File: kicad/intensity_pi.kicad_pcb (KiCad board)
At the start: 4 copper layers, 62.8 x 172 mm, 126 parts, among them J1 Input A, J2 Input B / Setpoint, J3 Monitor, J4 Output, J7 select 1, J8 Screw_Terminal_01x03, Q1 2N7002E, Q2 2N7002E, SW1 SW_SPDT, SW2 SW_SPDT, SW3 SW_SPDT, SW5 EG6100-ND, U1 LM4040DBZ-5, U10 OPA189, U11 PC817, U12 OPA189, U13 BUF634A, U14 TMUX6123, U17 TMUX6123, U18 OPA189, U19 L7815, U2 LM4040DBZ-5, U20 OPA189, U21 OPA189, U22 4x Comparator, U23 L7915, U3 INA849, U4 INA849, U5 OPA189, U7 OPA189, U8 BUF634A, U9 LM317_TO-252

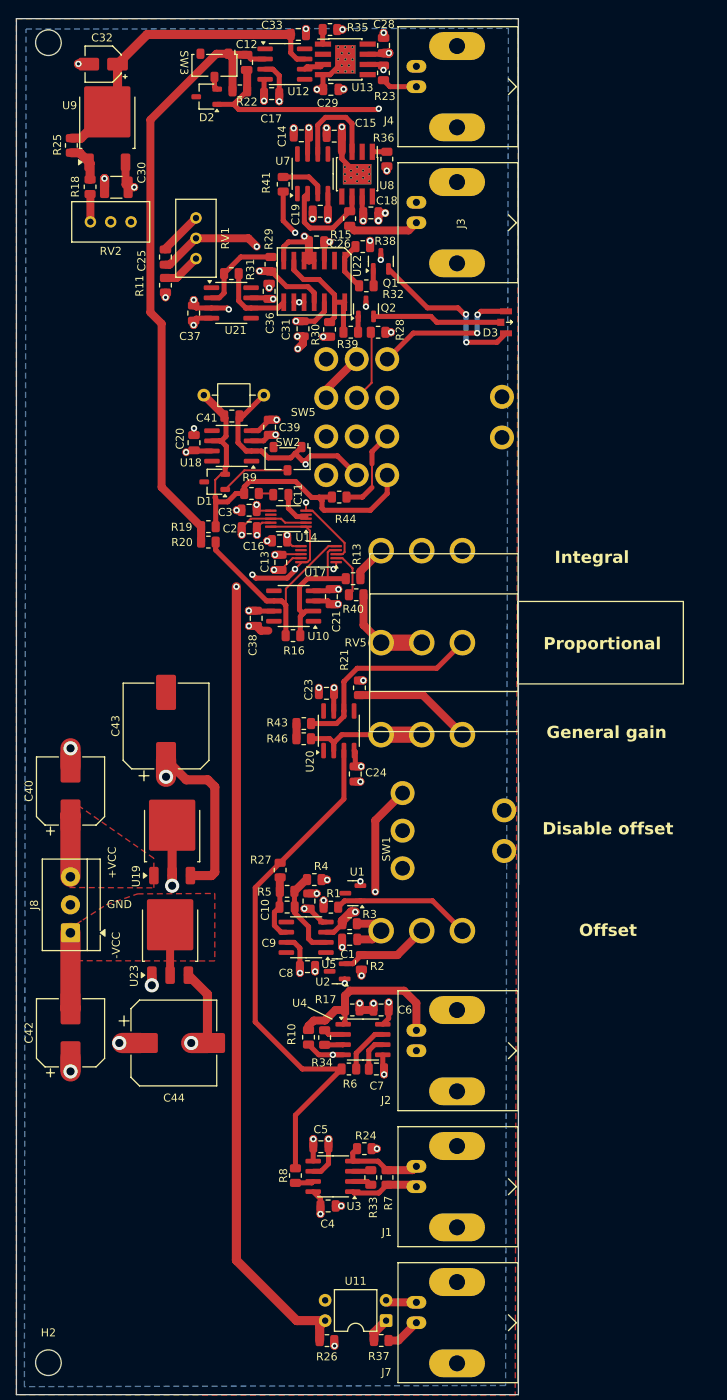
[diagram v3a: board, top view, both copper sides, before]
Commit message: Removal of antennas and other changes
The following edits has been made:
1) Simplification of certain critical traces
2) Removal of all antennas. Antennas are large traces connected to high
   impedance nodes. I'm quite strict about what high impedance means.
   Anything larger than a few Ohm can be considered high impedance.
3) Added labels most silkscreen labels where outside the physical board
   area
4) Added a thermal area to force

TO DO:
1) Add explanation near to all switches and trimpots
2) Check DRC
3) Add some GND vias
4) Check very carefully gerbers to see if any obvious manifacturing
   issue emerges
5) Send gerbers to fabrication.
6) Consider OPA209 or OPA140 for some of the opamps in the board.
One of the design choices of this board is that some opamps don't have
resistors for input current compensation. This is related to the choice
of the OPA189 for all board opamps (OPA189 has pA input current). It
turns out that for precision opamps manufacturers are starting to
discourage the use of resistors. Look at this [note](https://www.analog.com/en/resources/analog-dialogue/studentzone/studentzone-june-2017.html)
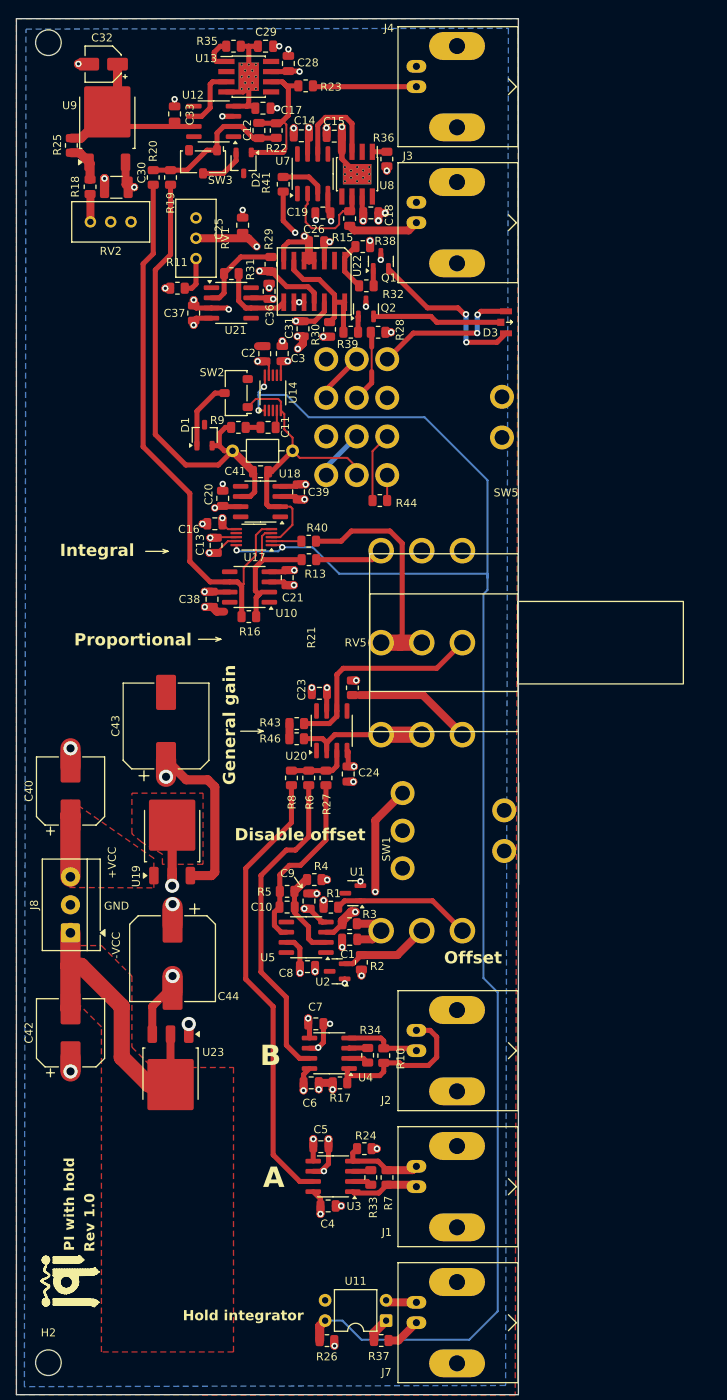
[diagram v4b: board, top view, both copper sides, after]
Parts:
- added REF**: , Custom_Footprints:JQI_LOGO_POSITIVE-SILKSCREEN, F.Cu at (-40.0, 68.3)
- moved R8 49.7 mm to (-15.6, 1.91)
- moved R20 46.1 mm to (-32.9, -73.2), turned to 90 degrees
- moved R19 43.9 mm to (-30.7, -73.2), turned to 90 degrees
- moved R6 36.7 mm to (-13.5, 1.91), turned to 90 degrees
- moved C2 21.9 mm to (-19.0, -51.1), turned to 90 degrees
- moved C3 20.0 mm to (-16.8, -51.1), turned to -90 degrees
- moved C33 18.4 mm to (-30.2, -81.1), turned to 90 degrees
- moved U23 17.5 mm to (-30.7, 39.0), turned to -90 degrees
- moved U14 15.8 mm to (-17.9, -46.2), turned to 90 degrees
- moved R27 12.9 mm to (-11.3, 1.91)
- moved C6 12.6 mm to (-13.2, 40.0), turned to 0 degrees
- moved U13 12.3 mm to (-21.0, -85.7)
- moved R35 12.2 mm to (-22.9, -89.6)
- moved SW3 12.1 mm to (-26.7, -75.1)
- moved C28 12.1 mm to (-16.0, -87.4)
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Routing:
- net Net-(U14C-SEL1): track 127.0 -> 206.1 mm
- net Net-(SW3-A): track 78.3 -> 19.5 mm
- net Net-(U20-+): track 66.5 -> 7.85 mm
- net Input_A: track 2.29 -> 56.4 mm
- net Net-(R16-Pad2): track 26.9 -> 71.0 mm
- net Input_B: track 6.26 -> 40.5 mm
- net Net-(D1-A): track 50.2 -> 83.3 mm
- net -V_DC_unregulated: track 15.8 -> 38.1 mm
- net Net-(R40-Pad1): track 12.0 -> 29.5 mm
- net Vlim+: track 38.1 -> 22.1 mm
- net GND: track 99.3 -> 84.0 mm, vias 46 -> 50
- net Internal_setpoint: track 8.10 -> 22.8 mm
- net Net-(D2-K): track 33.0 -> 20.1 mm, vias 2 -> 0
- net Net-(J4-In): track 4.45 -> 13.0 mm
- net Error_signal: track 97.1 -> 104.1 mm
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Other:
- board text added: "A"
- board text added: "B"
- board text added: "Hold integrator"
- board text added: "PI with hold"
- board text added: "Rev 1.0"

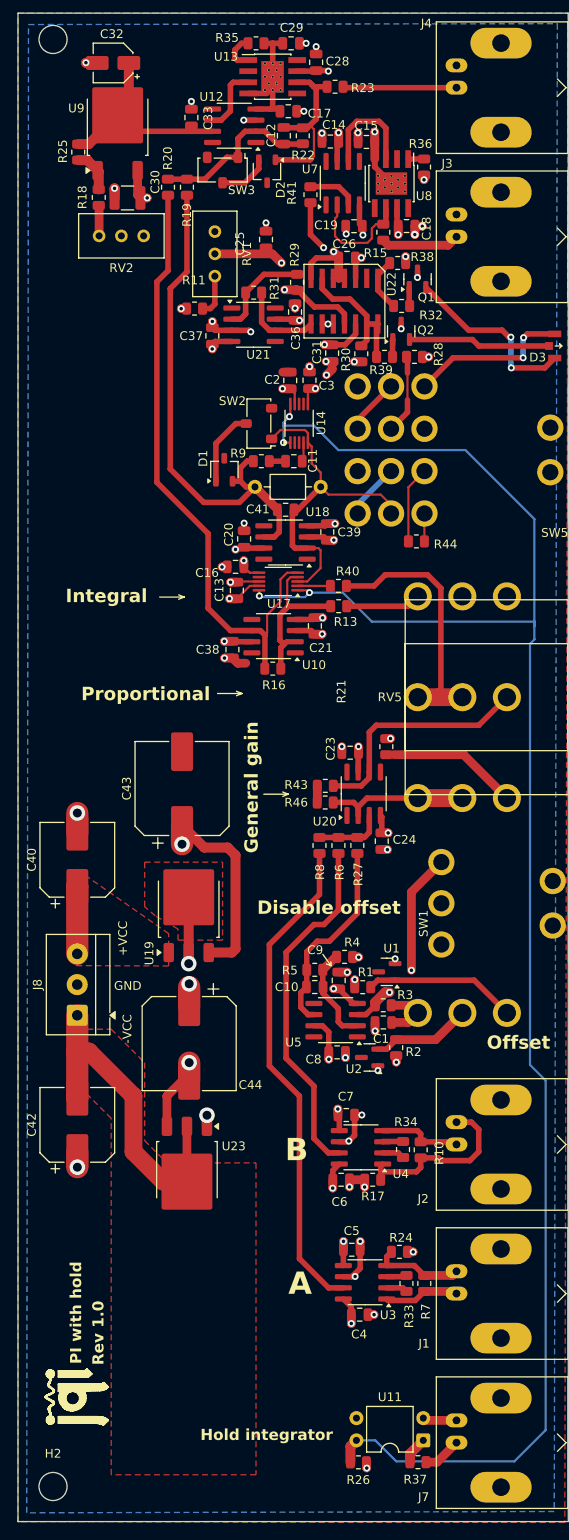
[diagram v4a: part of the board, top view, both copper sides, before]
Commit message: fixing missing traces and adding additional vias
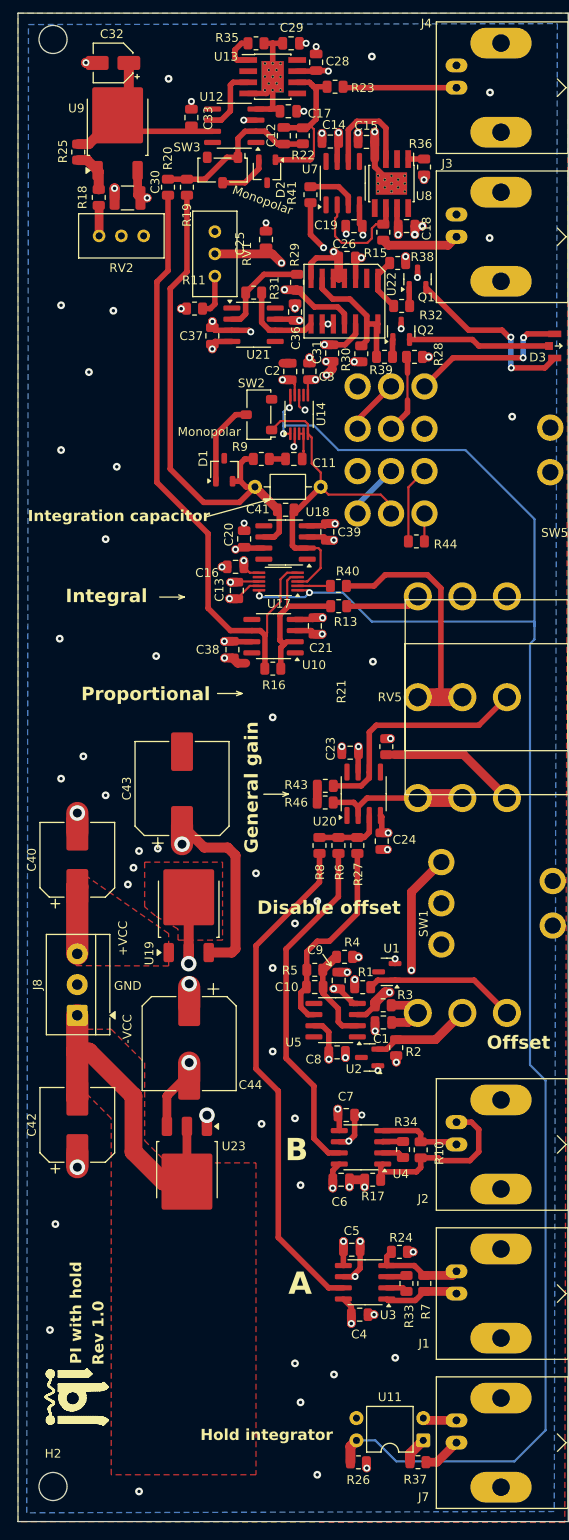
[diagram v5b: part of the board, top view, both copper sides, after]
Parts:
- moved C2 1.02 mm to (-19.0, -52.1)
- moved C3 1.02 mm to (-16.8, -52.2)
- moved SW2 1.02 mm to (-22.5, -47.2)
- moved U14 1.02 mm to (-17.9, -47.2)
- moved C11 0.25 mm to (-18.5, -42.2)
- moved R9 0.25 mm to (-22.2, -42.2)
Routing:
- net GND: track 84.0 -> 87.0 mm, vias 50 -> 90
- net Net-(C11-Pad1): track 2.18 -> 3.44 mm
- net Input_A: track 56.4 -> 57.6 mm
- net Net-(SW2-A): track 38.1 -> 39.1 mm
- net Net-(D1-K): track 8.70 -> 9.72 mm
- net Input_B: track 40.5 -> 39.9 mm
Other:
- board text added: "Integration capacitor"
- board text added: "Monopolar"

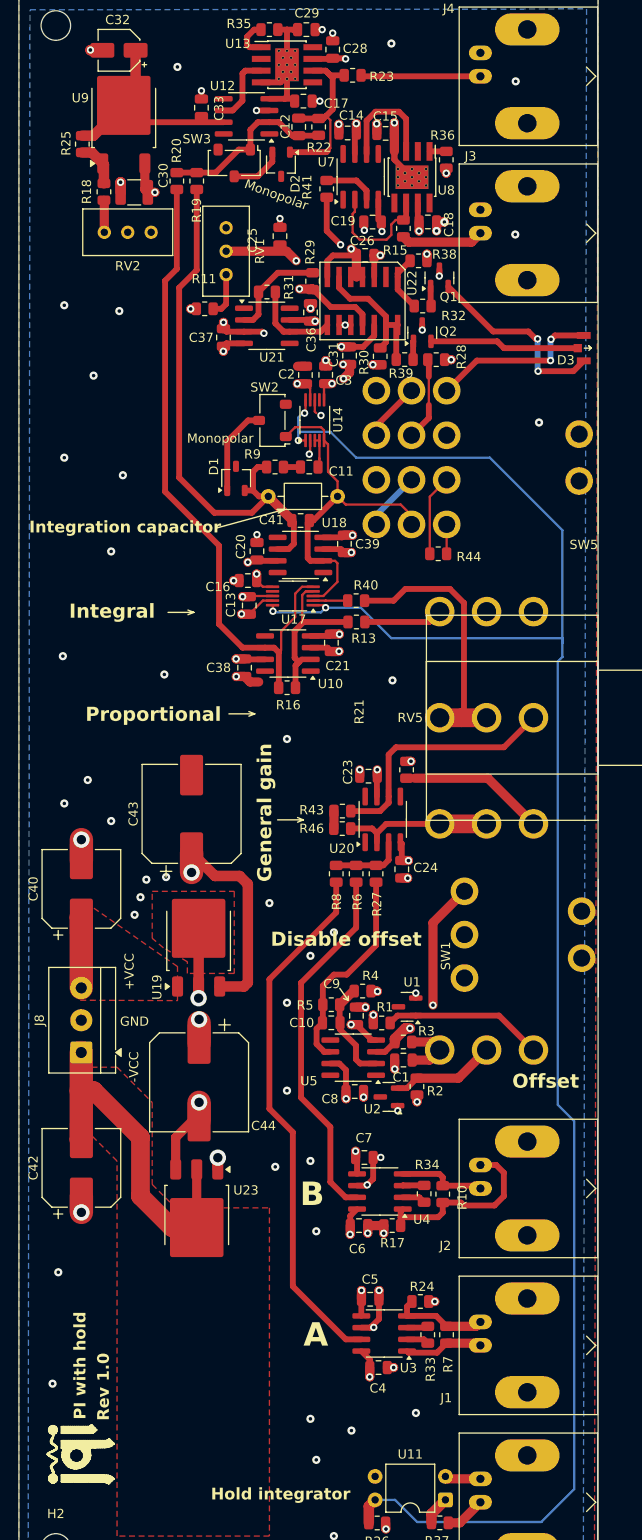
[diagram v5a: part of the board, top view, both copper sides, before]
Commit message: V1.1, Fixedincorrect footprints for Green/Red LED, Diodes, Mosfets, Flipped Input A/B Polarity, Potentiometer labels, Incorrect part nos for V regulators. No functionality changes
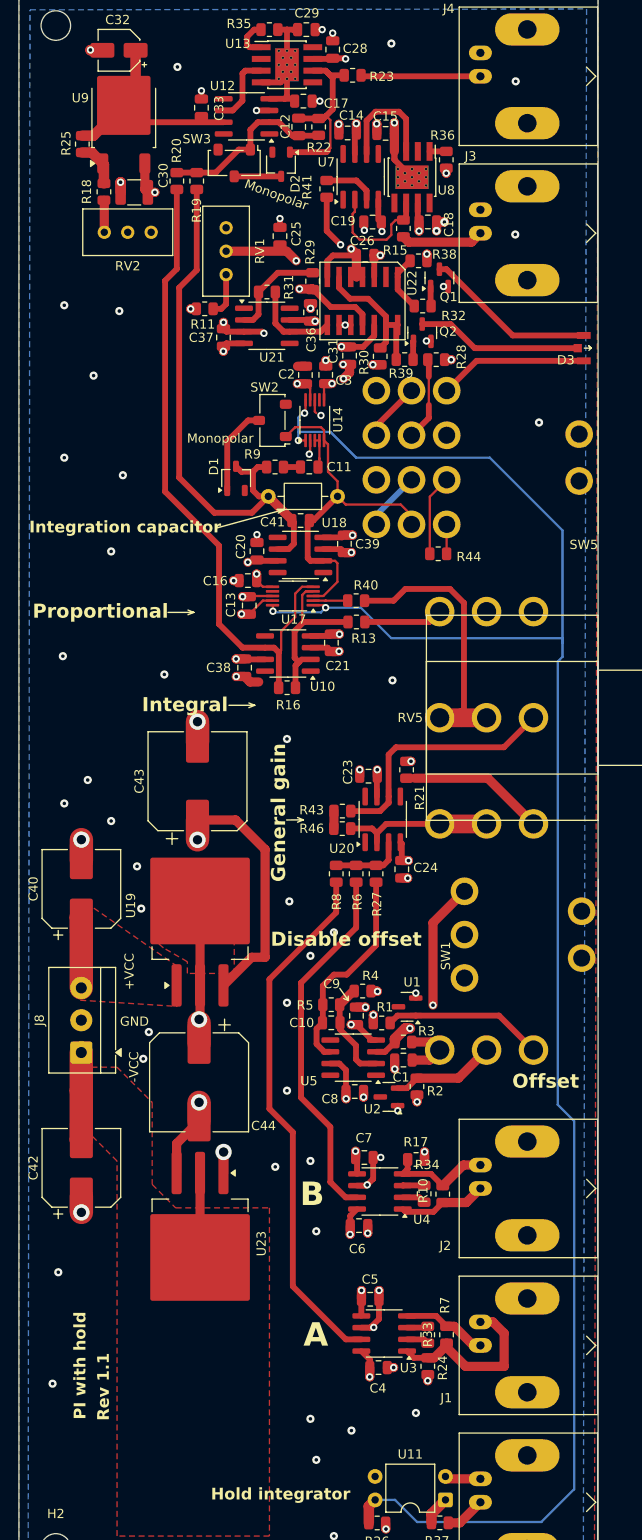
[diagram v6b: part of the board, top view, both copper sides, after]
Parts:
- removed REF**: , Custom_Footprints:JQI_LOGO_POSITIVE-SILKSCREEN
- SW5: value EG6100-ND -> SW_DP3T
- U19, U23: footprint Package_TO_SOT_SMD:TO-252-3_TabPin2 -> Package_TO_SOT_SMD:TO-263-3_TabPin2
- moved R17 7.62 mm to (-6.97, 32.9), turned to 180 degrees
- moved R24 7.06 mm to (-5.70, 55.3), turned to 90 degrees
- moved C43 3.60 mm to (-30.6, -8.12)
- moved U23 3.02 mm to (-30.4, 42.0)
- moved U19 2.73 mm to (-30.4, 6.35)
- turned R10 to -90 degrees
- turned R7 to 90 degrees
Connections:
- D1 pad 2: Net-(D1-A) -> (no net)
- D1 pad 3: (no net) -> Net-(D1-A)
- D2 pad 2: Net-(D2-A) -> (no net)
- D2 pad 3: (no net) -> Net-(D2-A)
- Q1 pad 2: Net-(D3-K1) -> GND
- Q1 pad 3: GND -> Net-(D3-K1)
- Q2 pad 2: Net-(D3-K2) -> GND
- Q2 pad 3: GND -> Net-(D3-K2)
- U3 pad 1: Net-(J1-In) -> Net-(J1-Ext)
- U3 pad 4: Net-(J1-Ext) -> Net-(J1-In)
- U4 pad 1: Net-(J2-Ext) -> Net-(J2-In)
- U4 pad 4: Net-(J2-In) -> Net-(J2-Ext)
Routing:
- net -V_DC_unregulated: track 38.1 -> 18.6 mm
- net Net-(J1-Ext): track 10.4 -> 19.6 mm
- net Net-(J2-Ext): track 20.3 -> 11.7 mm
- net GND: track 87.0 -> 93.4 mm
- net +15V: track 73.4 -> 78.0 mm
- net Vlim+: track 22.1 -> 19.5 mm
- net Net-(D3-A): track 28.3 -> 25.8 mm, vias 2 -> 0
- net Net-(D3-K1): track 21.0 -> 18.6 mm, vias 2 -> 0
- net Net-(U10--): track 20.7 -> 18.4 mm
- net Net-(D3-K2): track 16.2 -> 17.9 mm
- net Net-(D1-A): track 83.7 -> 84.9 mm
- net Net-(J1-In): track 8.21 -> 9.27 mm
- net Net-(SW5-Pad3): track 6.41 -> 5.39 mm
- net Net-(SW5-Pad11): track 6.41 -> 5.39 mm
- net Net-(SW2-A): track 39.1 -> 38.1 mm
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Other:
- board text added: "Rev 1.1"
- board text removed: "Rev 1.0"

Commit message: Updated schematic and design
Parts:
- removed C30: 10uF, Capacitor_SMD:C_1210_3225Metric
- removed C32: 22uF, Capacitor_SMD:CP_Elec_4x5.8
- removed C33: 100nF, Capacitor_SMD:C_0805_2012Metric
- added C22: 6p, Capacitor_SMD:C_0805_2012Metric, F.Cu at (-79.7, -60.7)
- added C27: 6p, Capacitor_SMD:C_0805_2012Metric, F.Cu at (-79.7, -57.7)
- added C34: 100nF, Capacitor_SMD:C_0805_2012Metric, F.Cu at (-79.7, -54.7)
- added C35: 100nF, Capacitor_SMD:C_0805_2012Metric, F.Cu at (-79.7, -51.7)
- added C46: 100nF, Capacitor_SMD:C_0805_2012Metric, F.Cu at (-79.7, -48.7)
- added D4: D, Package_TO_SOT_SMD:TSOT-23, F.Cu at (-84.6, -55.1)
- added D5: D, Package_TO_SOT_SMD:TSOT-23, F.Cu at (-84.6, -50.4)
- added D6: D, Package_TO_SOT_SMD:TSOT-23, F.Cu at (-84.6, -45.8)
- added J5: Sweep IN, Connector_Coaxial:BNC_Amphenol_B6252HB-NPP3G-50_Horizontal, F.Cu at (-129.8, -4.57)
- added R12: 10k, Resistor_SMD:R_0805_2012Metric, F.Cu at (-79.7, -45.7)
- added R14: 10k, Resistor_SMD:R_0805_2012Metric, F.Cu at (-79.7, -42.7)
- added R42: 10k, Resistor_SMD:R_0805_2012Metric, F.Cu at (-79.7, -39.8)
- added R45: 10k, Resistor_SMD:R_0805_2012Metric, F.Cu at (-75.3, -45.7)
- added R47: 10k, Resistor_SMD:R_0805_2012Metric, F.Cu at (-75.3, -42.7)
- added R48: 1k, Resistor_SMD:R_0805_2012Metric, F.Cu at (-75.3, -39.8)
- added R49: 1k, Resistor_SMD:R_0805_2012Metric, F.Cu at (-70.9, -45.7)
- added R50: 10k, Resistor_SMD:R_0805_2012Metric, F.Cu at (-70.9, -42.7)
- added R51: 10k, Resistor_SMD:R_0805_2012Metric, F.Cu at (-70.9, -39.8)
- added R52: 1k, Resistor_SMD:R_0805_2012Metric, F.Cu at (-119.2, -31.5)
- added R53: DNP, Resistor_SMD:R_0805_2012Metric, F.Cu at (-119.2, -28.6)
- added R54: 10k, Resistor_SMD:R_0805_2012Metric, F.Cu at (-119.2, -25.6)
- added R55: 5k, Resistor_SMD:R_0805_2012Metric, F.Cu at (-119.2, -22.7)
- added R56: 10k, Resistor_SMD:R_0805_2012Metric, F.Cu at (-119.2, -19.7)
- added R57: 10k, Resistor_SMD:R_0805_2012Metric, F.Cu at (-119.2, -16.8)
- added RV6: 100k, Potentiometer_THT:Potentiometer_Bourns_3296W_Vertical, F.Cu at (-69.4, -59.0)
- added RV7: 100k, Potentiometer_THT:Potentiometer_Bourns_3296W_Vertical, F.Cu at (-69.4, -52.6)
- added RV9: 100k, Custom_Footprints:Bourns Circular Pots, B.Cu at (-91.3, -116.6)
- added SW4: SW_SPDT, Custom_Footprints:TDD DIP Switch, F.Cu at (-79.2, -34.8)
- added U26: OPA189, Package_SO:SOIC-8_3.9x4.9mm_P1.27mm, F.Cu at (-91.5, -52.3)
- added U27: OPA189, Package_SO:SOIC-8_3.9x4.9mm_P1.27mm, F.Cu at (-91.5, -45.7)
- added U32: OPA189, Package_SO:SOIC-8_3.9x4.9mm_P1.27mm, F.Cu at (-91.5, -39.1)
- added U33: INA849, Package_SO:SOIC-8_3.9x4.9mm_P1.27mm, F.Cu at (-106.5, -28.3)
- added U6: OPA189, Package_SO:SOIC-8_3.9x4.9mm_P1.27mm, F.Cu at (-107.8, -37.9)
- R18: value 1k -> 10k
- R25: value 330 -> 10k
- RV2: value 2k -> 100k; footprint Potentiometer_THT:Potentiometer_Bourns_3296W_Vertical -> Custom_Footprints:Bourns Circular Pots
- U9: value LM317_TO-252 -> OPA189; footprint Package_TO_SOT_SMD:TO-252-2 -> Package_SO:SOIC-8_3.9x4.9mm_P1.27mm
- moved R25 87.3 mm to (-119.2, -34.5), turned to 0 degrees
- moved RV2 86.9 mm to (-125.9, -50.5), turned to 0 degrees
- moved R18 85.7 mm to (-119.2, -37.4), turned to 0 degrees
- moved D2 64.8 mm to (-84.6, -59.8), turned to 0 degrees
- moved U9 57.0 mm to (-91.5, -58.9), turned to 0 degrees
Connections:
- C12 pad 1: Net-(D2-K) -> Net-(U13-OUT)
- C12 pad 2: Net-(SW3-A) -> Net-(D4-K)
- R18 pad 1: Net-(R18-Pad1) -> Net-(J5-Ext)
- R18 pad 2: Net-(U9-ADJ) -> Net-(J5-In)
- R19 pad 2: Net-(SW3-A) -> Net-(U6-+)
- R20 pad 2: Net-(SW3-A) -> Net-(U6-+)
- R22 pad 1: Net-(SW3-A) -> Net-(D4-K)
- R22 pad 2: Net-(D2-K) -> Net-(U13-OUT)
- R23 pad 1: Net-(D2-K) -> Net-(U13-OUT)
- R25 pad 1: Net-(U9-ADJ) -> Net-(U6--)
- R25 pad 2: Vlim+ -> V_PI_OUT
- R28 pad 2: Net-(R28-Pad2) -> Net-(D3-A)
- RV2 pad 1: Net-(R18-Pad1) -> Net-(R56-Pad2)
- RV2 pad 2: GND -> Net-(R56-Pad2)
- RV2 pad 3: GND -> Net-(R55-Pad1)
- SW3 pad 1: Net-(SW3-A) -> V_CLAMP_N
- SW3 pad 2: Net-(D2-A) -> GND
- SW5 pad 10: Net-(D3-A) -> (no net)
- SW5 pad 12: Net-(D3-A) -> (no net)
- SW5 pad 7: unconnected-(SW5-Pad7) -> (no net)
- SW5 pad 8: Net-(R28-Pad2) -> (no net)
- U12 pad 2: Net-(SW3-A) -> Net-(D4-K)
- U12 pad 7: Vlim+ -> +15V
- U13 pad 6: Net-(D2-K) -> Net-(U13-OUT)
- U9 pad 1: Net-(U9-ADJ) -> unconnected-(U9-NC-Pad1)
- U9 pad 2: Vlim+ -> Net-(U9--)
- U9 pad 3: +15V -> V_CLAMP_P
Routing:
- net Net-(U13-OUT): track 0.00 -> 20.1 mm
- net Net-(D2-K): track 20.1 -> 0.00 mm
- net Vlim+: track 19.5 -> 0.00 mm
- net V_CLAMP_N: track 0.00 -> 19.5 mm
- net Net-(SW3-A): track 19.5 -> 0.00 mm
- net Net-(R28-Pad2): track 8.86 -> 0.00 mm
- net Net-(D3-A): track 25.8 -> 34.7 mm
- net Net-(D2-A): track 5.08 -> 0.00 mm
- net Net-(U9-ADJ): track 4.91 -> 0.00 mm
- net +15V: track 78.0 -> 74.0 mm, vias 21 -> 20
- net Net-(R18-Pad1): track 3.49 -> 0.00 mm
- net GND: track 93.4 -> 95.2 mm, vias 90 -> 88
